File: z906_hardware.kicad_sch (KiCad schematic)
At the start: 64 parts, among them J1 USB_C_Receptacle_USB2.0_14P, J2 AudioJack3, J3 DE_15 Amplifier, J4 DE15 Console, U1 ESP32-S3-WROOM-1, U2 TPS62A02APDDC, U3 PCM5102A, U4 TPD2EUSB30, U5 TPD1E05U06DYA, U6 TPS7A4533, U7 PCM1860DBT, U8 TPD2E2U06DCK

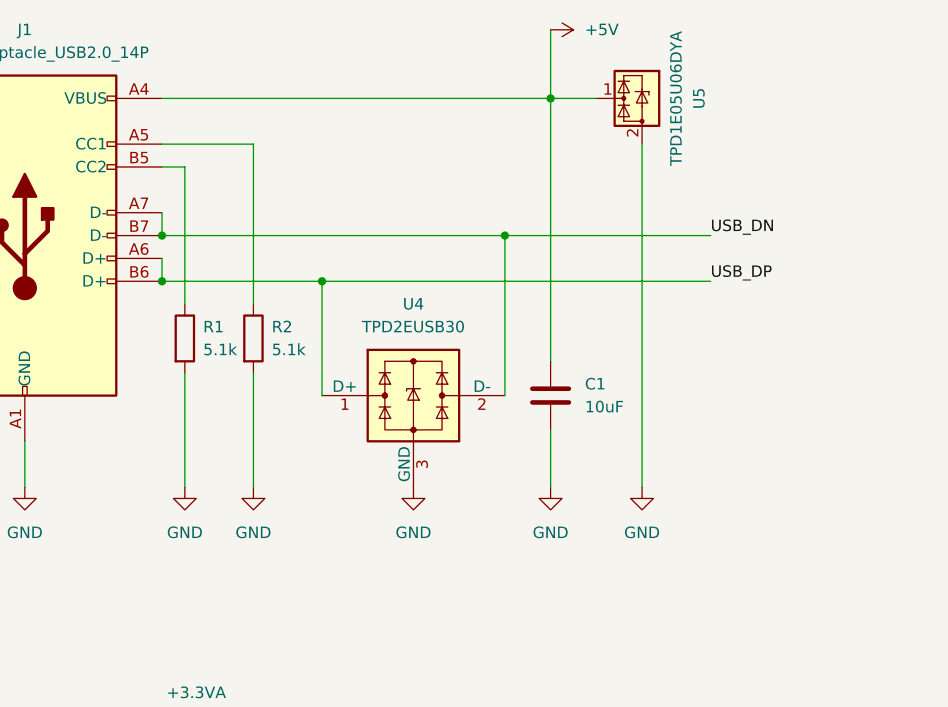
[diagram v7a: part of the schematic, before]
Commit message: add polyfuse to vbus
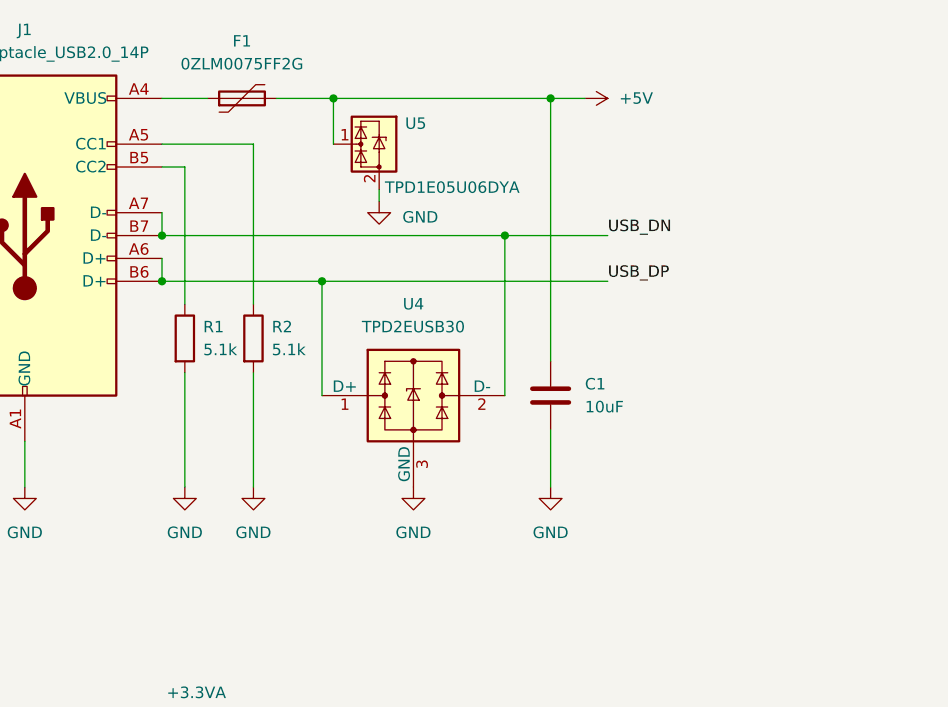
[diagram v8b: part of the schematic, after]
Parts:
- added F1: 0ZLM0075FF2G, symbol Device:Polyfuse
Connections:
- net +5V: now also F1.2; no longer J1.A4 (VBUS), J1.A9 (VBUS), J1.B4 (VBUS), J1.B9 (VBUS)
- new net: F1.1, J1.A4 (VBUS), J1.A9 (VBUS), J1.B4 (VBUS), J1.B9 (VBUS)
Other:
- moved on the sheet: U5
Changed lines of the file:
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@@
 	)
 	(junction
+		(at 44.45 46.99)
+		(diameter 0)
+		(color 0 0 0 0)
+	)
+	(junction
 		(at 347.98 76.2)
 		(diameter 0)
@@
 	)
 	(junction
-		(at 111.76 184.15)
+		(at 63.5 26.67)
 		(diameter 0)
 		(color 0 0 0 0)
 	)
 	(junction
-		(at 48.26 109.22)
+		(at 111.76 184.15)
 		(diameter 0)
 		(color 0 0 0 0)
 	)
 	(junction
-		(at 44.45 46.99)
+		(at 48.26 109.22)
 		(diameter 0)
 		(color 0 0 0 0)
@@
 	)
 	(junction
-		(at 82.55 41.91)
-		(diameter 0)
-		(color 0 0 0 0)
-	)
-	(junction
 		(at 158.75 148.59)
 		(diameter 0)
@@
 	)
 	(junction
-		(at 87.63 26.67)
-		(diameter 0)
-		(color 0 0 0 0)
-	)
-	(junction
 		(at 163.83 151.13)
 		(diameter 0)
@@
 	)
 	(junction
+		(at 82.55 41.91)
+		(diameter 0)
+		(color 0 0 0 0)
+	)
+	(junction
 		(at 323.85 38.1)
 		(diameter 0)
@@
 	)
 	(junction
+		(at 87.63 26.67)
+		(diameter 0)
+		(color 0 0 0 0)
+	)
+	(junction
 		(at 297.18 38.1)
 		(diameter 0)
@@
 	(wire
 		(pts
+			(xy 57.15 26.67) (xy 63.5 26.67)
+		)
+		(stroke
+			(width 0)
+			(type default)
+		)
+	)
+	(wire
+		(pts
 			(xy 185.42 151.13) (xy 193.04 151.13)
 		)
@@
 	(wire
 		(pts
-			(xy 44.45 26.67) (xy 87.63 26.67)
-		)
-		(stroke
-			(width 0)
-			(type default)
-		)
-	)
-	(wire
-		(pts
 			(xy 322.58 191.77) (xy 342.9 191.77)
 		)
@@
 	(wire
 		(pts
+			(xy 68.58 36.83) (xy 68.58 38.1)
+		)
+		(stroke
+			(width 0)
+			(type default)
+		)
+	)
+	(wire
+		(pts
 			(xy 144.78 245.11) (xy 167.64 245.11)
 		)
@@
 	(wire
 		(pts
+			(xy 44.45 26.67) (xy 49.53 26.67)
+		)
+		(stroke
+			(width 0)
+			(type default)
+		)
+	)
+	(wire
+		(pts
 			(xy 330.2 124.46) (xy 340.36 124.46)
 		)
@@
 	(wire
 		(pts
-			(xy 97.79 31.75) (xy 97.79 69.85)
-		)
-		(stroke
-			(width 0)
-			(type default)
-		)
-	)
-	(wire
-		(pts
 			(xy 44.45 44.45) (xy 44.45 46.99)
 		)
@@
 	(wire
 		(pts
-			(xy 87.63 26.67) (xy 92.71 26.67)
-		)
-		(stroke
-			(width 0)
-			(type default)
-		)
-	)
-	(wire
-		(pts
 			(xy 276.86 133.35) (xy 276.86 134.62)
 		)
@@
 	(wire
 		(pts
-			(xy 87.63 19.05) (xy 87.63 26.67)
+			(xy 322.58 173.99) (xy 342.9 173.99)
 		)
 		(stroke
@@
 	(wire
 		(pts
-			(xy 322.58 173.99) (xy 342.9 173.99)
+			(xy 67.31 181.61) (xy 67.31 184.15)
 		)
 		(stroke
@@
 	(wire
 		(pts
-			(xy 67.31 181.61) (xy 67.31 184.15)
+			(xy 297.18 38.1) (xy 299.72 38.1)
 		)
 		(stroke
@@
 	(wire
 		(pts
-			(xy 297.18 38.1) (xy 299.72 38.1)
+			(xy 313.69 234.95) (xy 313.69 237.49)
 		)
 		(stroke
@@
 	(wire
 		(pts
-			(xy 313.69 234.95) (xy 313.69 237.49)
+			(xy 158.75 162.56) (xy 158.75 148.59)
 		)
 		(stroke
@@
 	(wire
 		(pts
-			(xy 158.75 162.56) (xy 158.75 148.59)
+			(xy 161.29 38.1) (xy 163.83 38.1)
 		)
 		(stroke
@@
 	(wire
 		(pts
-			(xy 161.29 38.1) (xy 163.83 38.1)
+			(xy 63.5 31.75) (xy 63.5 26.67)
 		)
 		(stroke
@@
 	(wire
 		(pts
-			(xy 82.55 41.91) (xy 105.41 41.91)
+			(xy 82.55 41.91) (xy 93.98 41.91)
 		)
 		(stroke
@@
 	(wire
 		(pts
+			(xy 91.44 26.67) (xy 87.63 26.67)
+		)
+		(stroke
+			(width 0)
+			(type default)
+		)
+	)
+	(wire
+		(pts
 			(xy 87.63 135.89) (xy 97.79 135.89)
 		)
@@
 	(wire
 		(pts
-			(xy 44.45 46.99) (xy 105.41 46.99)
+			(xy 44.45 46.99) (xy 93.98 46.99)
 		)
 		(stroke
@@
 	(wire
 		(pts
+			(xy 63.5 26.67) (xy 87.63 26.67)
+		)
+		(stroke
+			(width 0)
+			(type default)
+		)
+	)
+	(wire
+		(pts
 			(xy 367.03 88.9) (xy 370.84 88.9)
 		)
@@
 	)
 	(label "USB_DP"
-		(at 105.41 46.99 0)
+		(at 93.98 46.99 0)
 		(effects
 			(font
@@
 	)
 	(label "USB_DN"
-		(at 105.41 41.91 0)
+		(at 93.98 41.91 0)
 		(effects
 			(font
@@
 	(symbol
 		(lib_id "power:+5V")
-		(at 87.63 19.05 270)
+		(at 91.44 26.67 270)
 		(unit 1)
 		(body_style 1)
@@
 		(fields_autoplaced yes)
 		(property "Reference" "#PWR011"
-			(at 83.82 19.05 0)
+			(at 87.63 26.67 0)
 			(hide yes)
 			(show_name no)
@@
 		)
 		(property "Value" "+5V"
-			(at 91.44 19.0499 90)
+			(at 95.25 26.6699 90)
 			(show_name no)
 			(do_not_autoplace no)
@@
 		)
 		(property "Footprint" ""
-			(at 87.63 19.05 0)
+			(at 91.44 26.67 0)
 			(hide yes)
 			(show_name no)
@@
 		)
 		(property "Datasheet" ""
-			(at 87.63 19.05 0)
+			(at 91.44 26.67 0)
 			(hide yes)
 			(show_name no)
@@
 		)
 		(property "Description" "Power symbol creates a global label with name \"+5V\""
-			(at 87.63 19.05 0)
+			(at 91.44 26.67 0)
 			(hide yes)
 			(show_name no)
@@
 	)
 	(symbol
+		(lib_id "Device:Polyfuse")
+		(at 53.34 26.67 90)
+		(unit 1)
+		(body_style 1)
+		(exclude_from_sim no)
+		(in_bom yes)
+		(on_board yes)
+		(in_pos_files yes)
+		(dnp no)
+		(fields_autoplaced yes)
+		(property "Reference" "F1"
+			(at 53.34 20.32 90)
+			(show_name no)
+			(do_not_autoplace no)
+			(effects
+				(font
+					(size 1.27 1.27)
+				)
+			)
+		)
+		(property "Value" "0ZLM0075FF2G"
+			(at 53.34 22.86 90)
+			(show_name no)
+			(do_not_autoplace no)
+			(effects
+				(font
+					(size 1.27 1.27)
+				)
+			)
+		)
+		(property "Footprint" ""
+			(at 58.42 25.4 0)
+			(hide yes)
+			(show_name no)
+			(do_not_autoplace no)
+			(effects
+				(font
+					(size 1.27 1.27)
+				)
+				(justify left)
+			)
+		)
+		(property "Datasheet" ""
+			(at 53.34 26.67 0)
+			(hide yes)
+			(show_name no)
+			(do_not_autoplace no)
+			(effects
+				(font
+					(size 1.27 1.27)
+				)
+			)
+		)
+		(property "Description" "Resettable fuse, polymeric positive temperature coefficient"
+			(at 53.34 26.67 0)
+			(hide yes)
+			(show_name no)
+			(do_not_autoplace no)
+			(effects
+				(font
+					(size 1.27 1.27)
+				)
+			)
+		)
+		(pin "2"
+		)
+		(pin "1"
+		)
+		(instances
+			(project "z906_hardware"
+				(path "/eb724320-f684-4550-84c5-ad44b13c3624"
+					(reference "F1")
+					(unit 1)
+				)
+			)
+		)
+	)
+	(symbol
 		(lib_id "power:GND")
 		(at 53.34 255.27 0)
@@
 	(symbol
 		(lib_id "Power_Protection:TPD1E05U06DYA")
-		(at 97.79 26.67 270)
+		(at 68.58 31.75 270)
 		(unit 1)
 		(body_style 1)
@@
 		(dnp no)
 		(property "Reference" "U5"
-			(at 104.14 26.67 0)
+			(at 72.644 29.464 90)
 			(show_name no)
 			(do_not_autoplace no)
@@
 		)
 		(property "Value" "TPD1E05U06DYA"
-			(at 101.6 26.67 0)
+			(at 76.708 36.576 90)
 			(show_name no)
 			(do_not_autoplace no)
@@
 		)
 		(property "Footprint" "Diode_SMD:D_SOD-523"
-			(at 93.345 29.21 0)
+			(at 64.135 34.29 0)
 			(hide yes)
 			(show_name no)
@@
 		)
 		(property "Datasheet" "https://www.ti.com/lit/ds/symlink/tpd1e05u06.pdf"
-			(at 91.44 29.21 0)
+			(at 62.23 34.29 0)
 			(hide yes)
 			(show_name no)
@@
 		)
 		(property "Description" "1-Channel ESD Protection for Super-Speed USB 3.0 Interface, SOD-523"
-			(at 97.79 26.67 0)
+			(at 68.58 31.75 0)
 			(hide yes)
 			(show_name no)
@@
 	(symbol
 		(lib_id "power:GND")
-		(at 97.79 69.85 0)
+		(at 68.58 38.1 0)
 		(unit 1)
 		(body_style 1)
@@
 		(in_pos_files yes)
 		(dnp no)
-		(fields_autoplaced yes)
 		(property "Reference" "#PWR01"
-			(at 97.79 76.2 0)
+			(at 68.58 44.45 0)
 			(hide yes)
 			(show_name no)
@@
 		)
 		(property "Value" "GND"
-			(at 97.79 74.93 0)
+			(at 73.152 39.878 0)
 			(show_name no)
 			(do_not_autoplace no)
@@
 		)
 		(property "Footprint" ""
-			(at 97.79 69.85 0)
+			(at 68.58 38.1 0)
 			(hide yes)
 			(show_name no)
@@
 		)
 		(property "Datasheet" ""
-			(at 97.79 69.85 0)
+			(at 68.58 38.1 0)
 			(hide yes)
 			(show_name no)
@@
 		)
 		(property "Description" "Power symbol creates a global label with name \"GND\" , ground"
-			(at 97.79 69.85 0)
+			(at 68.58 38.1 0)
 			(hide yes)
 			(show_name no)
